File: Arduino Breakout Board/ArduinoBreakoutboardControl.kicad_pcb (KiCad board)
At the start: 2 copper layers, 47.8 x 86.7 mm, 137 parts

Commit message: added an updated schematic with cleanner wire routing and updated the pcb for the schematic
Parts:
- removed BNO-055: Conn_01x04_Male, Connector_JST:JST_EH_B4B-EH-A_1x04_P2.50mm_Vertical
- added U2: BNO-555, SCR_Parts_Library:BNO055, F.Cu at (177.9, 85.7)
- J1: renamed from ENCODER (R)
- J2: renamed from ENCODER (L)
- moved PAD 0.13 mm to (162.6, 84.3)
- renumbered L289N to J3, 5V to J4, 5v to J5, A1 to U1
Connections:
- net Net-(A1-Pad23) renamed SDA
- net Net-(A1-Pad25) renamed SCL
- J1 pad 1: Net-(A1-Pad27) -> +5V
- J1 pad 3: Net-(A1-Pad10) -> RIghtA
- J1 pad 4: Net-(A1-Pad6) -> RightB
- J2 pad 1: Net-(A1-Pad27) -> +5V
- J2 pad 3: Net-(A1-Pad5) -> LeftA
- J2 pad 4: Net-(A1-Pad7) -> LeftB
- J3 pad 1: Net-(A1-Pad8) -> ENA
- J3 pad 2: Net-(A1-Pad9) -> ENB
- J3 pad 3: Net-(A1-Pad11) -> IN1
- J3 pad 4: Net-(A1-Pad12) -> IN2
- J3 pad 5: Net-(A1-Pad13) -> IN3
- J3 pad 6: Net-(A1-Pad15) -> IN4
- J4 pad 2: Net-(A1-Pad30) -> Net-(J4-Pad2)
- J5 pad 2: Net-(A1-Pad30) -> Net-(J4-Pad2)
- PAD pad 1: Net-(A1-Pad27) -> +5V
- U1 pad 1: Net-(A1-Pad1) -> Net-(U1-Pad1)
- U1 pad 10: Net-(A1-Pad10) -> RIghtA
- U1 pad 11: Net-(A1-Pad11) -> IN1
- U1 pad 12: Net-(A1-Pad12) -> IN2
- U1 pad 13: Net-(A1-Pad13) -> IN3
- U1 pad 14: Net-(A1-Pad14) -> Net-(U1-Pad14)
- U1 pad 15: Net-(A1-Pad15) -> IN4
- U1 pad 16: Net-(A1-Pad16) -> Net-(U1-Pad16)
- U1 pad 17: Net-(A1-Pad17) -> Net-(U1-Pad17)
- U1 pad 18: Net-(A1-Pad18) -> Net-(U1-Pad18)
- U1 pad 19: Net-(A1-Pad19) -> Net-(U1-Pad19)
- U1 pad 2: Net-(A1-Pad2) -> Net-(U1-Pad2)
- U1 pad 20: Net-(A1-Pad20) -> Net-(U1-Pad20)
- U1 pad 21: Net-(A1-Pad21) -> Net-(U1-Pad21)
- U1 pad 22: Net-(A1-Pad22) -> Net-(U1-Pad22)
- U1 pad 24: Net-(A1-Pad24) -> Net-(U1-Pad24)
- U1 pad 26: Net-(A1-Pad26) -> Net-(U1-Pad26)
- U1 pad 27: Net-(A1-Pad27) -> +5V
- U1 pad 28: Net-(A1-Pad28) -> Net-(U1-Pad28)
- U1 pad 3: Net-(A1-Pad3) -> Net-(U1-Pad3)
- U1 pad 30: Net-(A1-Pad30) -> Net-(J4-Pad2)
- U1 pad 5: Net-(A1-Pad5) -> LeftA
- U1 pad 6: Net-(A1-Pad6) -> RightB
- U1 pad 7: Net-(A1-Pad7) -> LeftB
- U1 pad 8: Net-(A1-Pad8) -> ENA
- U1 pad 9: Net-(A1-Pad9) -> ENB
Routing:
- net SDA: track 19.4 -> 3.18 mm
- net SCL: track 3.18 -> 11.8 mm
- net Net-(A1-Pad24): track 9.62 -> 3.18 mm
- net GND: track 4.49 -> 3.69 mm
- removed copper zone on B.Cu, net GND

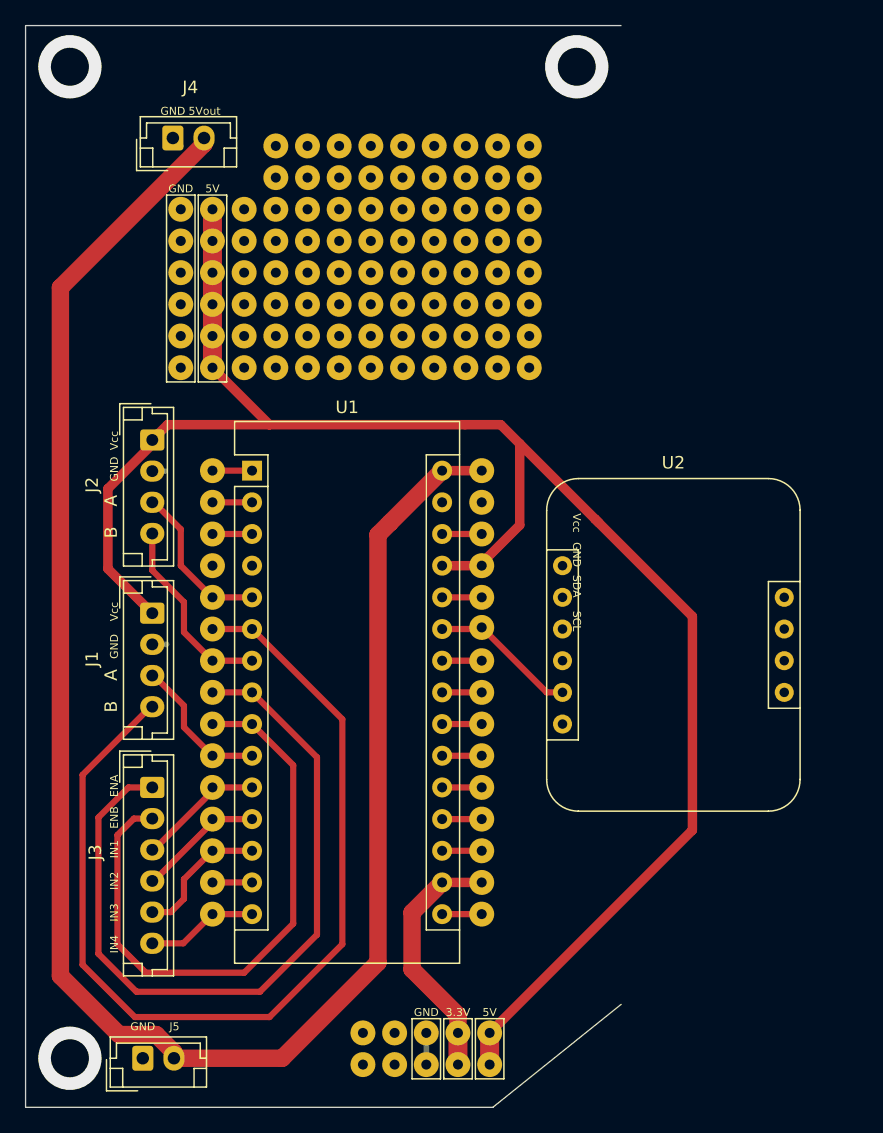
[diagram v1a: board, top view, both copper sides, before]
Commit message: started work on v2 of the Breakout board
Added Schematic for v2 of the Board

Updated PCB to address the changes done to the Schematic
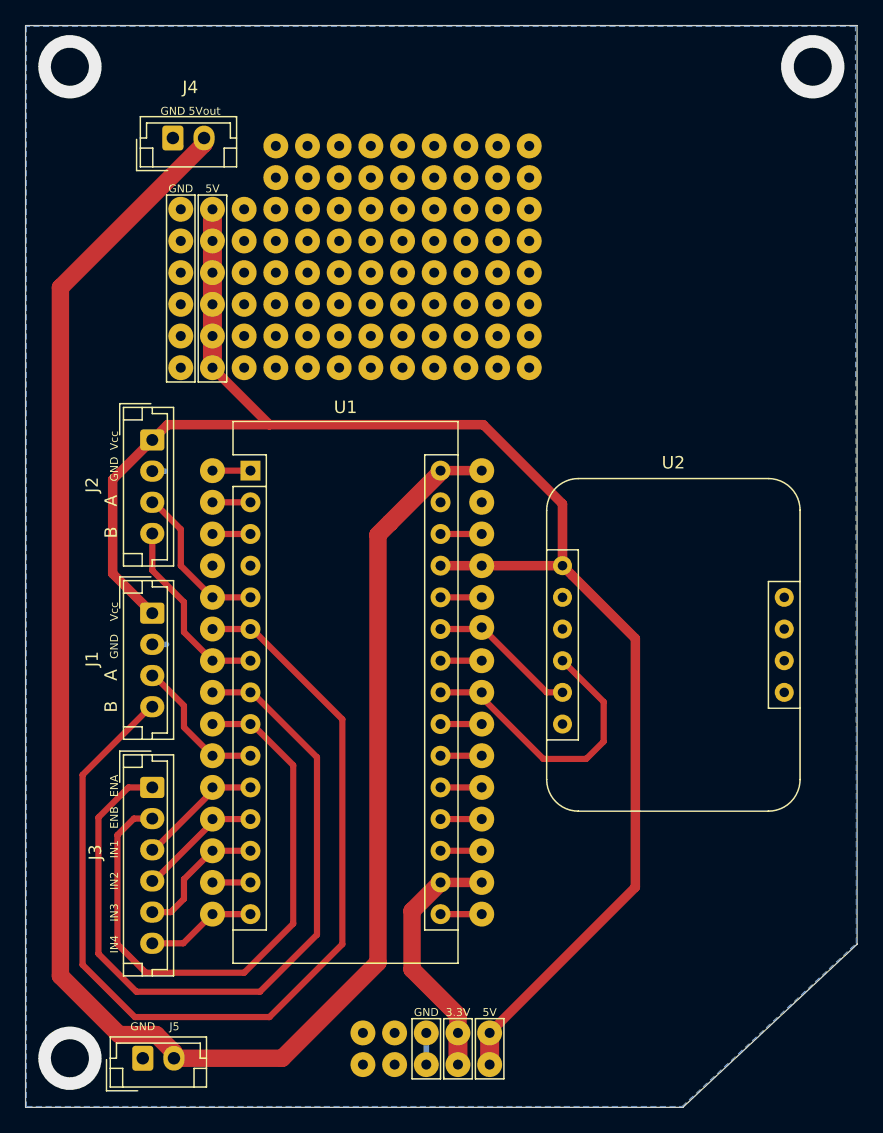
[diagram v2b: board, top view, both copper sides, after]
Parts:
- moved U1 0.13 mm to (144.0, 71.8)
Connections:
- PAD pad 1: Net-(A1-Pad8) -> ENA
- PAD pad 1: Net-(A1-Pad6) -> RightB
- PAD pad 1: Net-(A1-Pad16) -> Net-(U1-Pad16)
- PAD pad 1: Net-(A1-Pad22) -> Net-(U1-Pad22)
- PAD pad 1: Net-(A1-Pad17) -> Net-(U1-Pad17) (x3)
- PAD pad 1: Net-(A1-Pad21) -> Net-(U1-Pad21)
- PAD pad 1: Net-(A1-Pad24) -> Net-(U1-Pad24)
- PAD pad 1: Net-(A1-Pad27) -> +5V (x8)
- PAD pad 1: Net-(A1-Pad19) -> Net-(U1-Pad19)
- PAD pad 1: Net-(A1-Pad26) -> Net-(U1-Pad26)
- PAD pad 1: Net-(A1-Pad18) -> Net-(U1-Pad18)
- PAD pad 1: Net-(A1-Pad28) -> Net-(U1-Pad28)
- PAD pad 1: Net-(A1-Pad30) -> Net-(J4-Pad2)
- PAD pad 1: Net-(A1-Pad15) -> IN4
- PAD pad 1: Net-(A1-Pad13) -> IN3
- PAD pad 1: Net-(A1-Pad12) -> IN2
- PAD pad 1: Net-(A1-Pad10) -> RIghtA
- PAD pad 1: Net-(A1-Pad9) -> ENB
- PAD pad 1: Net-(A1-Pad3) -> Net-(U1-Pad3)
- PAD pad 1: Net-(A1-Pad1) -> Net-(U1-Pad1)
- PAD pad 1: Net-(A1-Pad2) -> Net-(U1-Pad2)
- PAD pad 1: Net-(A1-Pad5) -> LeftA
- PAD pad 1: Net-(A1-Pad7) -> LeftB
- PAD pad 1: Net-(A1-Pad14) -> Net-(U1-Pad14)
- PAD pad 1: Net-(A1-Pad11) -> IN1
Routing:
- net Net-(J4-Pad2): track 0.00 -> 148.7 mm
- net Net-(A1-Pad30): track 148.7 -> 0.00 mm
- net Net-(A1-Pad27): track 143.5 -> 0.00 mm
- net +5V: track 0.00 -> 133.8 mm
- net RightB: track 0.00 -> 79.6 mm
- net Net-(A1-Pad6): track 79.6 -> 0.00 mm
- net Net-(A1-Pad8): track 61.7 -> 0.00 mm
- net ENA: track 0.00 -> 61.7 mm
- net Net-(A1-Pad9): track 49.8 -> 0.00 mm
- net ENB: track 0.00 -> 49.8 mm
- net SDA: track 3.18 -> 23.8 mm
- net Net-(A1-Pad17): track 20.3 -> 0.00 mm
- net Net-(U1-Pad17): track 0.00 -> 20.3 mm
- net Net-(A1-Pad7): track 15.4 -> 0.00 mm
- net LeftB: track 0.00 -> 15.4 mm
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- added copper zone on B.Cu, net GND
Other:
- board size 47.8 x 86.7 mm -> 66.7 x 86.7 mm
- board text removed: "SCL"
- board text removed: "SDA"

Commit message: added 2 more connectors for servos to the schematic and PCB
Updated and finished the PCB for V2
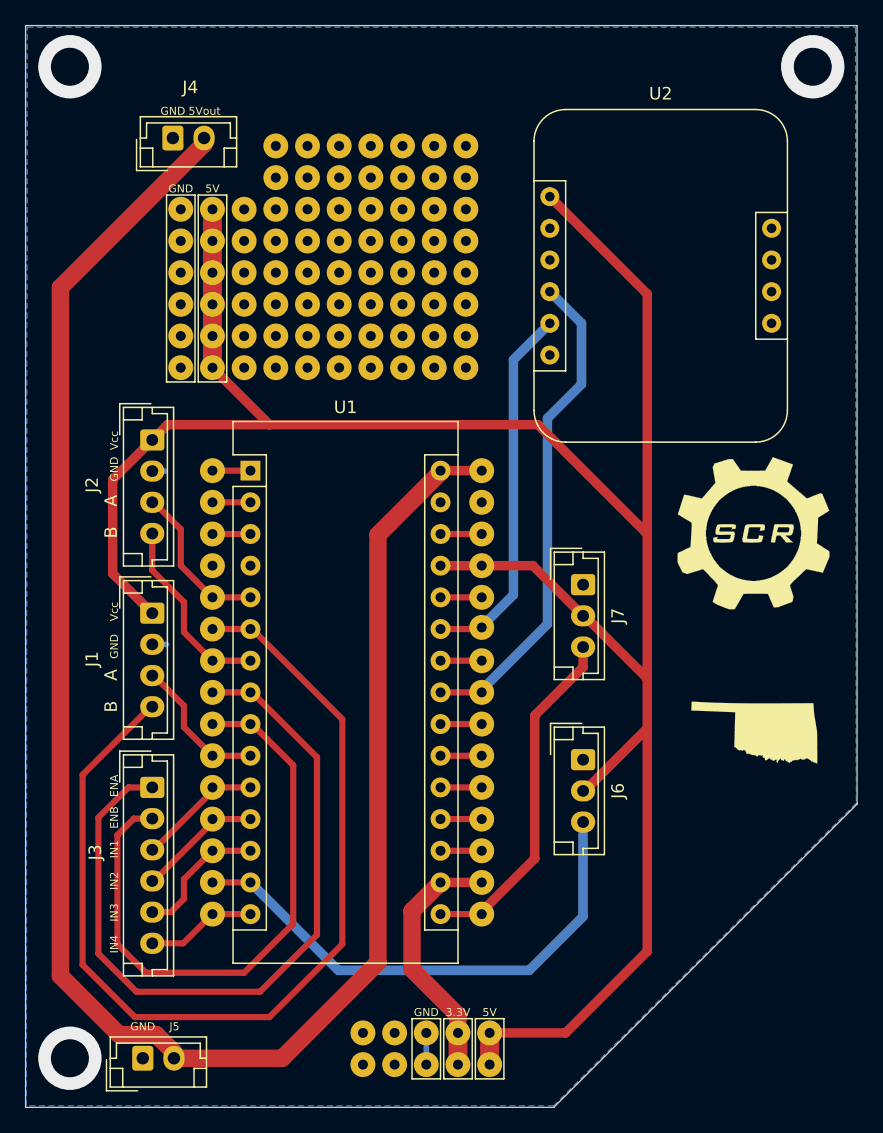
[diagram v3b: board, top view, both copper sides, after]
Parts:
- removed the PAD at (163.8, 53.3)
- removed the PAD at (166.4, 48.3)
- removed the PAD at (166.4, 53.3)
- removed the PAD at (163.8, 63.5)
- removed the PAD at (163.8, 61.0)
- removed the PAD at (163.8, 55.9)
- removed the PAD at (163.8, 50.8)
- removed the PAD at (163.8, 45.7)
- removed the PAD at (166.4, 61.0)
- removed the PAD at (166.4, 58.4)
- removed the PAD at (166.4, 50.8)
- removed the PAD at (166.4, 63.5)
- removed the PAD at (166.4, 45.7)
- removed the PAD at (163.8, 58.4)
- removed the PAD at (163.8, 48.3)
- removed the PAD at (166.4, 55.9)
- added G***: LOGO, SCR_Logos_Library:oklahoma-image, F.Cu at (184.4, 92.8)
- added G***: LOGO, SCR_Logos_Library:scr-logo, F.Cu at (184.3, 76.8)
- added J6: Conn_01x03, Connector_JST:JST_EH_B3B-EH-A_1x03_P2.50mm_Vertical, F.Cu at (170.7, 94.9)
- added J7: Conn_01x03, Connector_JST:JST_EH_B3B-EH-A_1x03_P2.50mm_Vertical, F.Cu at (170.7, 80.9)
- moved U2 29.6 mm to (176.9, 56.1)
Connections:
- net Net-(J4-Pad2) renamed +5VA
- net Net-(U1-Pad14) renamed SERV1
- net Net-(U1-Pad16) renamed SERV2
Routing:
- net +5V: track 133.8 -> 188.8 mm
- net SERV1: track 3.18 -> 42.1 mm
- net SERV2: track 3.18 -> 28.0 mm
- net SCL: track 11.8 -> 29.8 mm
- net SDA: track 23.8 -> 40.1 mm
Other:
- outline, holes or cut-outs redrawn

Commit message: Added silkscreen indicators for the servo motor JST
Added additional mounting holes
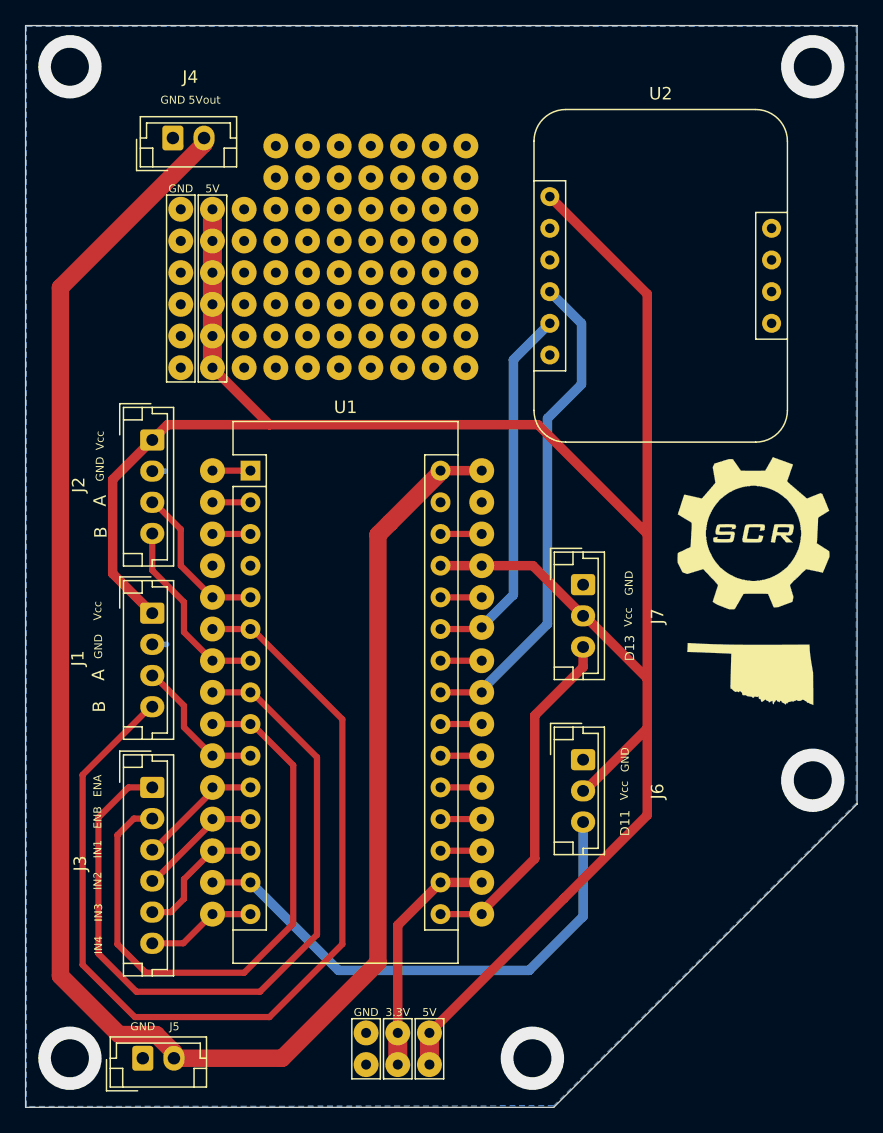
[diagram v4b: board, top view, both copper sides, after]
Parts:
- removed the PAD at (155.6, 119.4)
- removed the PAD at (153.0, 116.8)
- removed the PAD at (155.6, 116.8)
- removed the PAD at (153.0, 119.4)
- moved PAD 4.83 mm to (153.3, 116.8)
- moved PAD 4.83 mm to (153.3, 119.4)
- moved PAD 4.83 mm to (158.4, 116.8)
- moved PAD 4.83 mm to (155.8, 116.8)
- moved PAD 4.83 mm to (158.4, 119.4)
- moved PAD 4.83 mm to (155.8, 119.4)
- moved G*** 4.71 mm to (184.1, 88.1)
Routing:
- net GND: track 3.69 -> 1.15 mm
- net +5V: track 188.8 -> 187.2 mm
- net Net-(U1-Pad17): track 20.3 -> 19.2 mm
- net (no net): vias 3 -> 5
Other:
- board text added: "D11"
- board text added: "D13"
- board text added: "V 2.0"
- board text removed: "V 1.0"

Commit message: Changed pins of the servo to PWM pins
deleted unneccesary schematic files
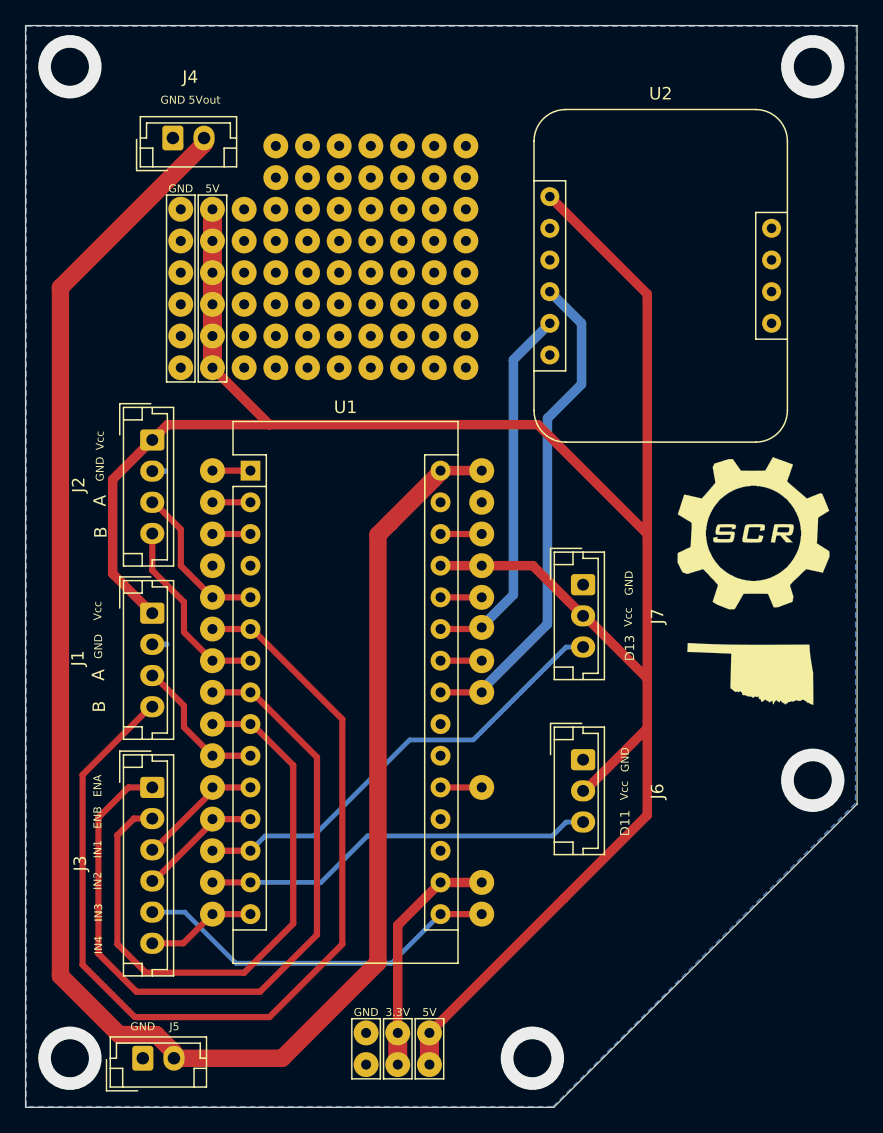
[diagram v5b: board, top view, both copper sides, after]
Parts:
- removed the PAD at (162.6, 92.1)
- removed the PAD at (162.6, 94.6)
- removed the PAD at (162.6, 99.7)
- removed the PAD at (162.6, 102.2)
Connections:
- PAD pad 1: SERV2 -> IN3
- PAD pad 1: Net-(A1-Pad20) -> Net-(U1-Pad20)
- PAD pad 1: IN3 -> SERV2
- U1 pad 13: IN3 -> SERV2
- U1 pad 16: SERV2 -> IN3
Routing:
- net IN3: track 11.0 -> 29.9 mm
- net SERV1: track 42.1 -> 31.9 mm
- net SERV2: track 28.0 -> 36.7 mm
- net Net-(U1-Pad22): track 3.18 -> 0.00 mm
- net Net-(U1-Pad21): track 3.18 -> 0.00 mm
- net Net-(U1-Pad20): track 0.00 -> 3.18 mm
- net Net-(U1-Pad19): track 3.18 -> 0.00 mm
- net Net-(U1-Pad18): track 3.18 -> 0.00 mm
- net Net-(A1-Pad20): track 3.18 -> 0.00 mm
